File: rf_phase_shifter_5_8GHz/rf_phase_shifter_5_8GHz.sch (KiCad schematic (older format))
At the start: 12 parts, among them J1 Conn_Coaxial, J2 Conn_Coaxial, J3 Conn_Coaxial

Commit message: update
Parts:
- removed FL1: C2327J5003AHF, C2327J5003AHF, symbol RF:C2327J5003AHF
- added FL1: C5060J5003AHF, analog_rf_phase_shifter_module:C5060J5003AHF, symbol analog_rf_phase_shifter_module:C5060J5003AHF
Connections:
- net GND: now also FL1.2 (GND_1), FL1.5 (GND_2)
- net at D1.1 (K), D3.1 (K), L1.2: now also FL1.6 (COUPLED)
- net at D2.1 (K), D4.1 (K), L2.2: now also FL1.4 (DIRECT)
- net at C1.1: now also FL1.1 (INPUT)
- net at C2.2: now also FL1.3 (ISOLATED)
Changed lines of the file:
@@
 EELAYER 30 0
 EELAYER END
-$Descr A4 11693 8268
+$Descr User 8268 5827
 encoding utf-8
 Sheet 1 1
-Title ""
+Title "Analog RF phase shifter 5,7-5,8GHz"
 Date ""
-Rev ""
-Comp ""
+Rev "1.0.0"
+Comp "Marcin Wachowiak, Poland"
 Comment1 ""
 Comment2 ""
@@
 	4450 1950 4450 1900
 Connection ~ 3900 1900
-$Comp
-L RF:C2327J5003AHF FL1
-U 1 1 60586F9C
-P 2200 1700
-F 0 "FL1" H 2950 1965 50  0000 C CNN
-F 1 "C2327J5003AHF" H 2950 1874 50  0000 C CNN
-F 2 "C2327J5003AHF" H 3550 1800 50  0001 L CNN
-F 3 "https://componentsearchengine.com/Datasheets/1/C2327J5003AHF.pdf" H 3550 1700 50  0001 L CNN
-F 4 "Signal Conditioning 2.3-2.7GHz IL=.4dB 3dB 90 Deg." H 3550 1600 50  0001 L CNN "Description"
-F 5 "0.73" H 3550 1500 50  0001 L CNN "Height"
-F 6 "ANAREN" H 3550 1400 50  0001 L CNN "Manufacturer_Name"
-F 7 "C2327J5003AHF" H 3550 1300 50  0001 L CNN "Manufacturer_Part_Number"
-F 8 "620-C2327J5003AHF" H 3550 1200 50  0001 L CNN "Mouser Part Number"
-F 9 "https://www.mouser.com/Search/Refine.aspx?Keyword=620-C2327J5003AHF" H 3550 1100 50  0001 L CNN "Mouser Price/Stock"
-	1    2200 1700
-	1    0    0    -1
-$EndComp
 Wire Wire Line
 	5000 2250 5000 2300
@@
 Wire Notes Line
 	4000 1950 4300 1950
+$Comp
+L analog_rf_phase_shifter_module:C5060J5003AHF FL1
+U 1 1 60906106
+P 2200 1700
+F 0 "FL1" H 2950 1965 50  0000 C CNN
+F 1 "C5060J5003AHF" H 2950 1874 50  0000 C CNN
+F 2 "analog_rf_phase_shifter_module:C5060J5003AHF" H 3550 1800 50  0001 L CNN
+F 3 "https://componentsearchengine.com/Datasheets/1/C5060J5003AHF.pdf" H 3550 1700 50  0001 L CNN
+F 4 "Signal Conditioning 5-6GHz IL=.4dB 3dB 90 Deg." H 3550 1600 50  0001 L CNN "Description"
+F 5 "0.73" H 3550 1500 50  0001 L CNN "Height"
+F 6 "ANAREN" H 3550 1400 50  0001 L CNN "Manufacturer_Name"
+F 7 "C5060J5003AHF" H 3550 1300 50  0001 L CNN "Manufacturer_Part_Number"
+	1    2200 1700
+	1    0    0    -1
+$EndComp
 $EndSCHEMATC

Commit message: updated libs
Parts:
- removed J1, J2, J3: Conn_Coaxial, Connector_Coaxial:SMA_Samtec_SMA-J-P-X-ST-EM1_EdgeMount, symbol Connector:Conn_Coaxial
- added J1, J2, J3: CON-SMA-EDGE-S, analog_rf_phase_shifter_module:CON-SMA-EDGE-S, symbol analog_rf_phase_shifter_module:CON-SMA-EDGE-S
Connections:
- net GND: now also J1.2 (Ext), J2.2 (Ext), J3.2 (Ext)
- net at L1.1, L2.1: now also J3.1 (In)
- net at C2.1: now also J2.1 (In)
- net at C1.2: now also J1.1 (In)
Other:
- moved on the sheet: C1, C2, D1, D2, D3, D4, FL1, L1, L2

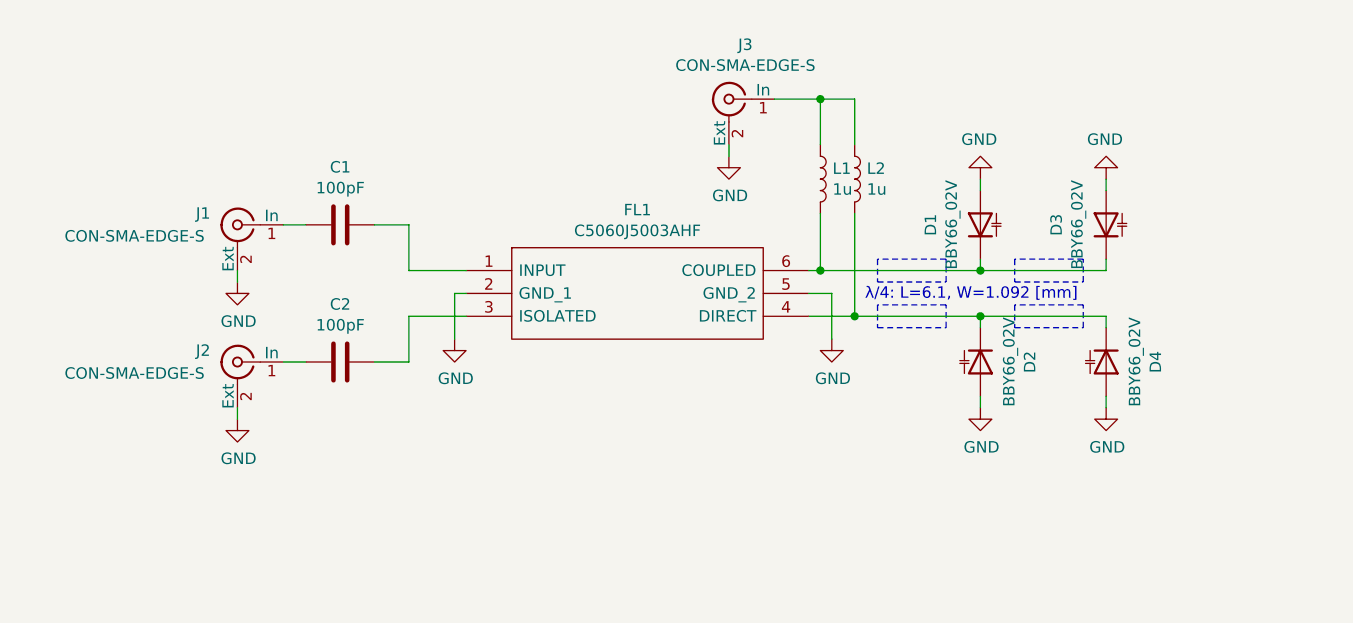
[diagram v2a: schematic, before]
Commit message: pcb init works
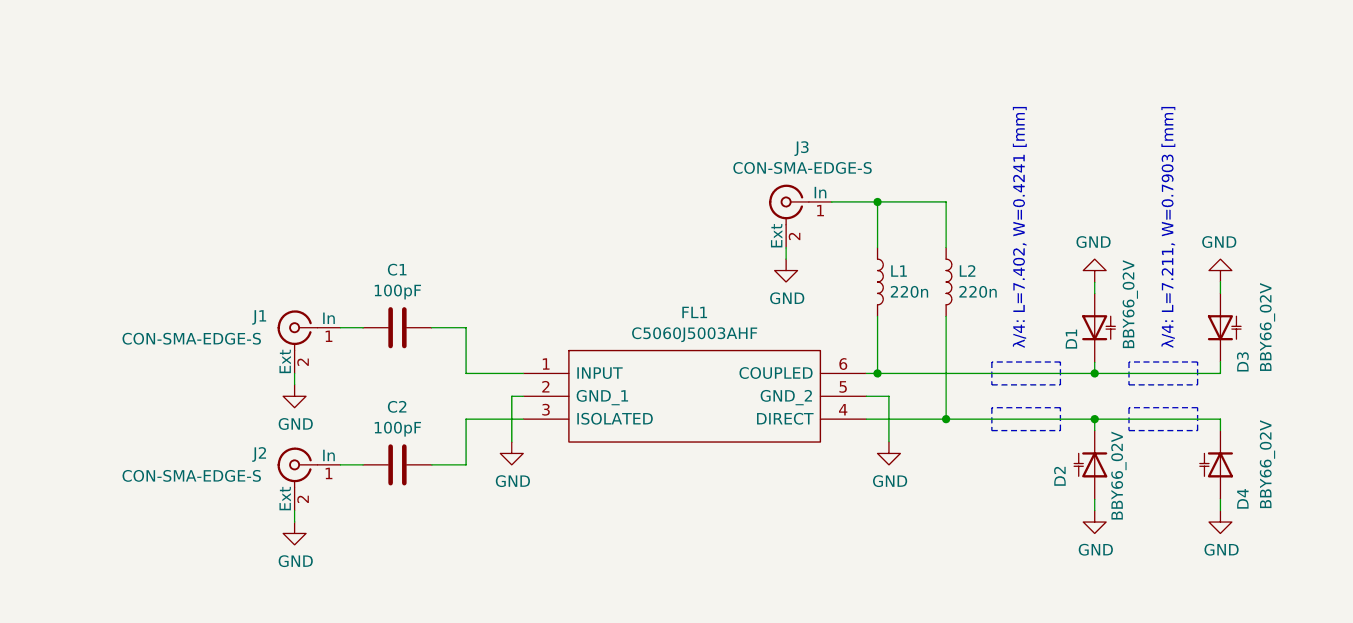
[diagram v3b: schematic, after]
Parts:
- L1, L2: value 1u -> 220n
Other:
- note added: "λ/4: L=7.211, W=0.7903 [mm]"
- note added: "λ/4: L=7.402, W=0.4241 [mm]"
- note removed: "λ/4: L=6.1, W=1.092 [mm]"
- moved on the sheet: C1, C2, D1, D2, D3, D4, FL1, J1, J2, J3, L1, L2

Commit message: finished pcb layouts
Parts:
- added TL1, TL2: TL_13_5_8GHz, analog_rf_phase_shifter_module:TL_13_5_8GHz, symbol analog_rf_phase_shifter_module:TL_13_5_8GHz
- added TL3, TL4: TL_24_5_8GHz, analog_rf_phase_shifter_module:TL_24_5_8GHz, symbol analog_rf_phase_shifter_module:TL_24_5_8GHz
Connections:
- net at FL1.6 (COUPLED), L1.2: now also TL1.1; no longer D1.1 (K), D3.1 (K)
- net at FL1.4 (DIRECT), L2.2: now also TL2.1; no longer D2.1 (K), D4.1 (K)
- new net: D1.1 (K), TL1.2, TL3.1
- new net: D2.1 (K), TL2.2, TL4.1
- new net: D3.1 (K), TL3.2
- new net: D4.1 (K), TL4.2
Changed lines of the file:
@@
 U 1 1 60375EF1
 P 5750 1900
-F 0 "D3" H 5600 1800 50  0000 C CNN
-F 1 "BBY66_02V" H 5750 1700 50  0000 C CNN
+F 0 "D3" H 5650 1800 50  0000 C CNN
+F 1 "BBY66_02V" H 5800 1700 50  0000 C CNN
 F 2 "Diode_SMD:D_SOD-523" H 5750 1900 50  0001 C CNN
 F 3 "~" H 5750 1900 50  0001 C CNN
@@
 $EndComp
 Wire Wire Line
-	5200 2100 5750 2100
+	5200 2100 5350 2100
 Wire Wire Line
-	5200 2300 5750 2300
+	5200 2300 5350 2300
 Wire Wire Line
-	4550 2300 5200 2300
+	4550 2300 4750 2300
 Connection ~ 5200 2100
 Wire Wire Line
-	4250 2100 5200 2100
+	4250 2100 4750 2100
 Text Notes 4900 2000 1    50   ~ 0
 λ/4: L=7.402, W=0.4241 [mm]
@@
 Wire Notes Line
 	4750 2350 5050 2350
+$Comp
+L analog_rf_phase_shifter_module:TL_13_5_8GHz TL1
+U 1 1 6151CF6D
+P 4900 2050
+F 0 "TL1" H 4650 2050 50  0000 C CNN
+F 1 "TL_13_5_8GHz" V 5000 2350 50  0000 C CNN
+F 2 "analog_rf_phase_shifter_module:TL_13_5_8GHz" H 4650 2200 50  0001 C CNN
+F 3 "" H 4650 2200 50  0001 C CNN
+	1    4900 2050
+	1    0    0    -1
+$EndComp
+Wire Wire Line
+	5050 2100 5200 2100
+$Comp
+L analog_rf_phase_shifter_module:TL_13_5_8GHz TL2
+U 1 1 6151D9C5
+P 4900 2250
+F 0 "TL2" H 4650 2250 50  0000 C CNN
+F 1 "TL_13_5_8GHz" H 4850 2100 50  0000 C CNN
+F 2 "analog_rf_phase_shifter_module:TL_13_5_8GHz" H 4650 2400 50  0001 C CNN
+F 3 "" H 4650 2400 50  0001 C CNN
+	1    4900 2250
+	1    0    0    -1
+$EndComp
+Wire Wire Line
+	5050 2300 5200 2300
+$Comp
+L analog_rf_phase_shifter_module:TL_24_5_8GHz TL3
+U 1 1 6151E660
+P 5500 2050
+F 0 "TL3" H 5275 1950 50  0000 C CNN
+F 1 "TL_24_5_8GHz" H 5950 1950 50  0000 C CNN
+F 2 "analog_rf_phase_shifter_module:TL_24_5_8GHz" H 5250 2200 50  0001 C CNN
+F 3 "" H 5250 2200 50  0001 C CNN
+	1    5500 2050
+	1    0    0    -1
+$EndComp
+Wire Wire Line
+	5650 2100 5750 2100
+$Comp
+L analog_rf_phase_shifter_module:TL_24_5_8GHz TL4
+U 1 1 6151EE61
+P 5500 2250
+F 0 "TL4" H 5275 2250 50  0000 C CNN
+F 1 "TL_24_5_8GHz" V 5500 1850 50  0000 C CNN
+F 2 "analog_rf_phase_shifter_module:TL_24_5_8GHz" H 5250 2400 50  0001 C CNN
+F 3 "" H 5250 2400 50  0001 C CNN
+	1    5500 2250
+	1    0    0    -1
+$EndComp
+Wire Wire Line
+	5650 2300 5750 2300
 $EndSCHEMATC

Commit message: added info about substrate thickness
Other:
- note added: "Substrate: FR4, thickness: 0.6 mm"
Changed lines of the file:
@@
 Wire Wire Line
 	5650 2300 5750 2300
+Text Notes 1625 3100 0    50   ~ 0
+Substrate: FR4, thickness: 0.6 mm
 $EndSCHEMATC

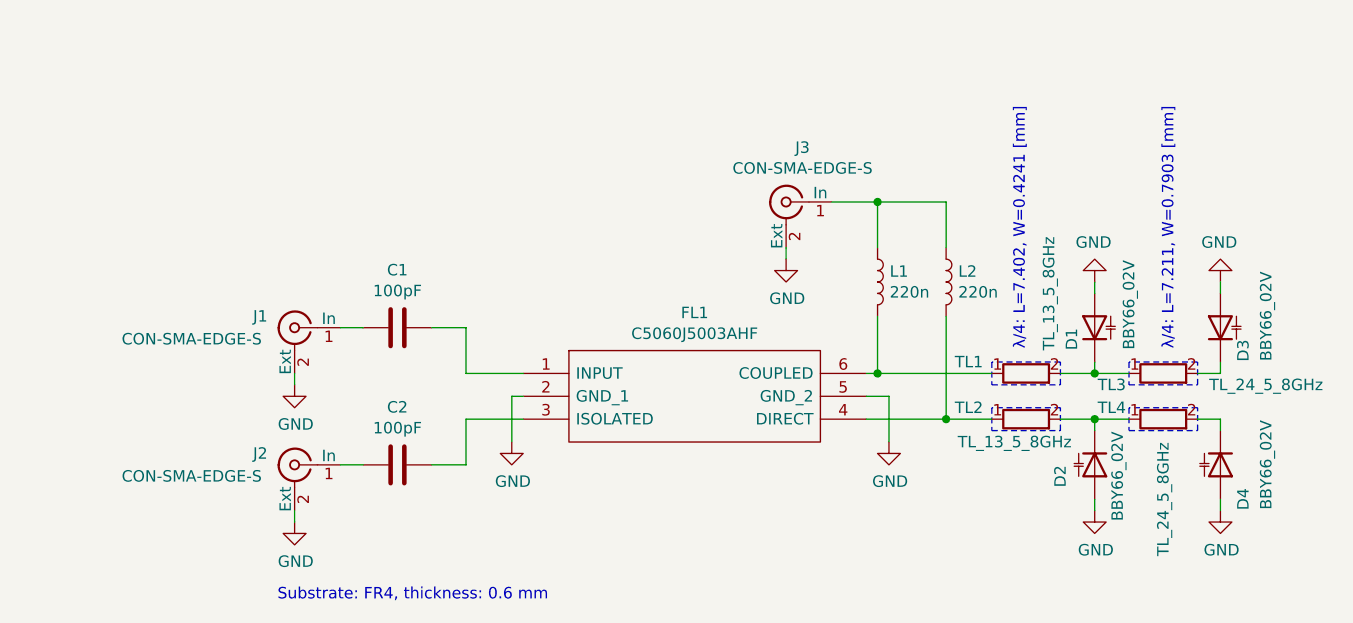
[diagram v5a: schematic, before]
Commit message: Finished layout of second prototypes
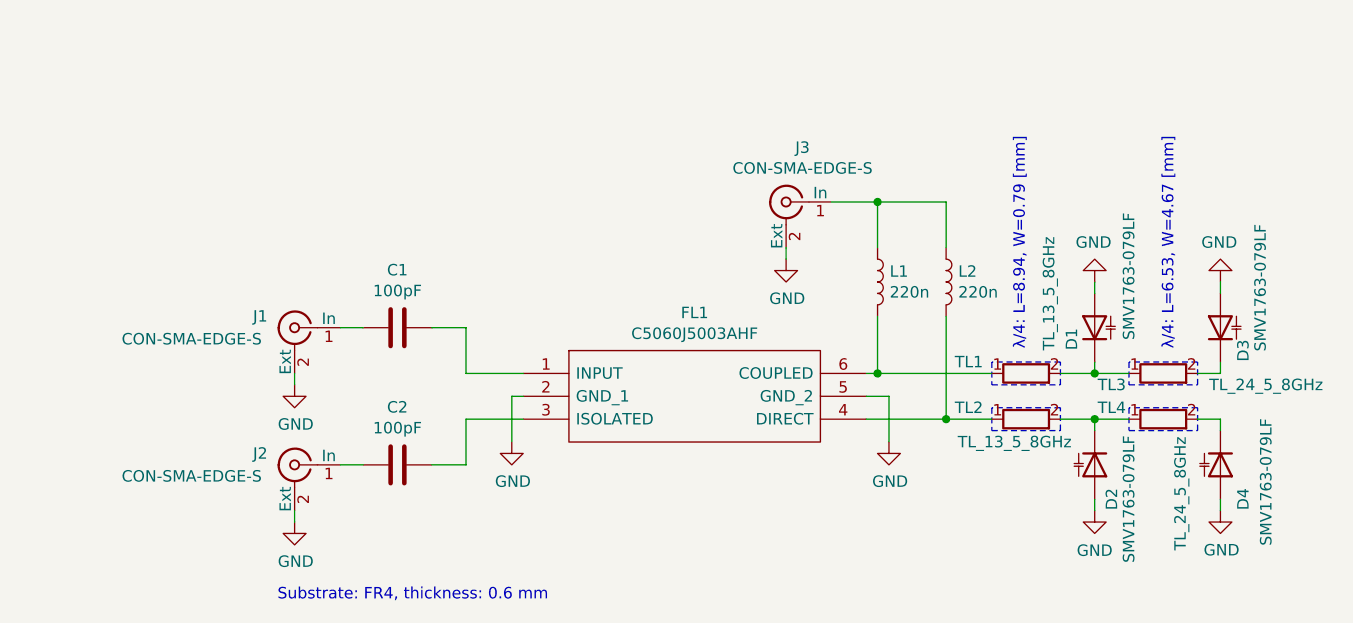
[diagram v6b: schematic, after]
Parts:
- D1, D2, D3, D4: value BBY66_02V -> SMV1763-079LF
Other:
- note added: "λ/4: L=6.53, W=4.67 [mm]"
- note added: "λ/4: L=8.94, W=0.79 [mm]"
- note removed: "λ/4: L=7.211, W=0.7903 [mm]"
- note removed: "λ/4: L=7.402, W=0.4241 [mm]"
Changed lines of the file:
@@
 $EndComp
 Text Notes 5550 2000 1    50   ~ 0
-λ/4: L=7.211, W=0.7903 [mm]
+λ/4: L=6.53, W=4.67 [mm]
 Wire Wire Line
 	5750 2300 5750 2350
@@
 $EndComp
 $Comp
-L power:GND #PWR0106
-U 1 1 605766D6
-P 5200 2700
-F 0 "#PWR0106" H 5200 2450 50  0001 C CNN
-F 1 "GND" H 5205 2527 50  0000 C CNN
-F 2 "" H 5200 2700 50  0001 C CNN
-F 3 "" H 5200 2700 50  0001 C CNN
-	1    5200 2700
-	1    0    0    -1
-$EndComp
-$Comp
 L Device:D_Capacitance D4
 U 1 1 60376509
 P 5750 2500
 F 0 "D4" H 5900 2600 50  0000 C CNN
-F 1 "BBY66_02V" H 5750 2700 50  0000 C CNN
+F 1 "SMV1763-079LF " H 5825 2700 50  0000 C CNN
 F 2 "Diode_SMD:D_SOD-523" H 5750 2500 50  0001 C CNN
 F 3 "~" H 5750 2500 50  0001 C CNN
@@
 	0    1    1    0
 $EndComp
-$Comp
-L Device:D_Capacitance D3
-U 1 1 60375EF1
-P 5750 1900
-F 0 "D3" H 5650 1800 50  0000 C CNN
-F 1 "BBY66_02V" H 5800 1700 50  0000 C CNN
-F 2 "Diode_SMD:D_SOD-523" H 5750 1900 50  0001 C CNN
-F 3 "~" H 5750 1900 50  0001 C CNN
-	1    5750 1900
-	0    -1   -1   0
-$EndComp
-$Comp
-L Device:D_Capacitance D2
-U 1 1 60375884
-P 5200 2500
-F 0 "D2" H 5250 2350 50  0000 C CNN
-F 1 "BBY66_02V" H 5250 2600 50  0000 C CNN
-F 2 "Diode_SMD:D_SOD-523" H 5200 2500 50  0001 C CNN
-F 3 "~" H 5200 2500 50  0001 C CNN
-	1    5200 2500
-	0    1    1    0
-$EndComp
-$Comp
-L Device:D_Capacitance D1
-U 1 1 60375266
-P 5200 1900
-F 0 "D1" H 5150 2000 50  0000 C CNN
-F 1 "BBY66_02V" H 5300 1750 50  0000 C CNN
-F 2 "Diode_SMD:D_SOD-523" H 5200 1900 50  0001 C CNN
-F 3 "~" H 5200 1900 50  0001 C CNN
-	1    5200 1900
-	0    -1   -1   0
-$EndComp
 Wire Wire Line
 	5200 2100 5350 2100
@@
 	4250 2100 4750 2100
 Text Notes 4900 2000 1    50   ~ 0
-λ/4: L=7.402, W=0.4241 [mm]
+λ/4: L=8.94, W=0.79 [mm]
 Wire Notes Line
 	4750 2150 5050 2150
@@
 P 5500 2250
 F 0 "TL4" H 5275 2250 50  0000 C CNN
-F 1 "TL_24_5_8GHz" V 5500 1850 50  0000 C CNN
+F 1 "TL_24_5_8GHz" V 5575 1875 50  0000 C CNN
 F 2 "analog_rf_phase_shifter_module:TL_24_5_8GHz" H 5250 2400 50  0001 C CNN
 F 3 "" H 5250 2400 50  0001 C CNN
@@
 Text Notes 1625 3100 0    50   ~ 0
 Substrate: FR4, thickness: 0.6 mm
+$Comp
+L Device:D_Capacitance D1
+U 1 1 60375266
+P 5200 1900
+F 0 "D1" H 5150 2000 50  0000 C CNN
+F 1 "SMV1763-079LF " H 5425 1750 50  0000 C CNN
+F 2 "Diode_SMD:D_SOD-523" H 5200 1900 50  0001 C CNN
+F 3 "~" H 5200 1900 50  0001 C CNN
+	1    5200 1900
+	0    -1   -1   0
+$EndComp
+$Comp
+L Device:D_Capacitance D2
+U 1 1 60375884
+P 5200 2500
+F 0 "D2" H 5350 2575 50  0000 C CNN
+F 1 "SMV1763-079LF " H 5350 2650 50  0000 C CNN
+F 2 "Diode_SMD:D_SOD-523" H 5200 2500 50  0001 C CNN
+F 3 "~" H 5200 2500 50  0001 C CNN
+	1    5200 2500
+	0    1    1    0
+$EndComp
+$Comp
+L power:GND #PWR0106
+U 1 1 605766D6
+P 5200 2700
+F 0 "#PWR0106" H 5200 2450 50  0001 C CNN
+F 1 "GND" H 5200 2525 50  0000 C CNN
+F 2 "" H 5200 2700 50  0001 C CNN
+F 3 "" H 5200 2700 50  0001 C CNN
+	1    5200 2700
+	1    0    0    -1
+$EndComp
+$Comp
+L Device:D_Capacitance D3
+U 1 1 60375EF1
+P 5750 1900
+F 0 "D3" H 5650 1800 50  0000 C CNN
+F 1 "SMV1763-079LF " H 5925 1725 50  0000 C CNN
+F 2 "Diode_SMD:D_SOD-523" H 5750 1900 50  0001 C CNN
+F 3 "~" H 5750 1900 50  0001 C CNN
+	1    5750 1900
+	0    -1   -1   0
+$EndComp
 $EndSCHEMATC
